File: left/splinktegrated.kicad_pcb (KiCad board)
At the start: 4 copper layers, 72.6 x 88.4 mm, 83 parts, among them J1 USB_C_Receptacle_USB2.0, J10 NA_Ribbon, J13 Conn_01x01_Socket, J14 Cirque, J15 Conn_01x01_Socket, J16 Conn_01x01_Socket, J17 Conn_01x01_Socket, J18 USB_C_Receptacle_USB2.0, J19 Conn_01x01_Socket, J20 Conn_01x01_Socket, J5 Conn_01x02, J6 Cirque, J7 NA_trackball, J8 NA_Ribbon, J9 NA_RGB, Q4 AO3401A, Q5 AO3401A, SW2 NA_SW_SPST, U1 RP2040, U2 USBLC6-2P6, U3 XC6210B332MR-G, U4 USBLC6-2P6, U5 W25Q128JVS, U6 74LVC1T45, Y1 Crystal_GND24

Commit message: vik logo
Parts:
- moved G*** 9.73 mm to (149.7, 130.2)
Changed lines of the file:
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@@
 	(footprint "LOGO"
 		(layer "F.Cu")
-		(at 159.35 130.95)
+		(at 149.65 130.18)
 		(property "Reference" "G***"
 			(at 0 0 0)

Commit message: routing
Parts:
- moved C6 0.17 mm to (156.5, 92.7)
- moved R6 0.16 mm to (157.8, 92.7)
- moved R7 0.16 mm to (159.1, 92.7)
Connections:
- J6 pad 10: SCL -> SDA
- J6 pad 9: SDA -> SCL
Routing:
- net SCL: track 49.6 -> 48.4 mm
- net SDA: track 49.7 -> 50.3 mm
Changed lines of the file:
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@@
 	(footprint "Resistor_SMD:R_0402_1005Metric"
 		(layer "F.Cu")
-		(at 157.8 92.53 -90)
+		(at 157.8 92.69 -90)
 		(descr "Resistor SMD 0402 (1005 Metric), square (rectangular) end terminal, IPC_7351 nominal, (Body size source: IPC-SM-782 page 72, https://www.pcb-3d.com/wordpress/wp-content/uploads/ipc-sm-782a_amendment_1_and_2.pdf), generated with kicad-footprint-generator")
 		(tags "resistor")
@@
 	(footprint "Resistor_SMD:R_0402_1005Metric"
 		(layer "F.Cu")
-		(at 159.1 92.85 -90)
+		(at 159.1 92.69 -90)
 		(descr "Resistor SMD 0402 (1005 Metric), square (rectangular) end terminal, IPC_7351 nominal, (Body size source: IPC-SM-782 page 72, https://www.pcb-3d.com/wordpress/wp-content/uploads/ipc-sm-782a_amendment_1_and_2.pdf), generated with kicad-footprint-generator")
 		(tags "resistor")
@@
 	(footprint "Capacitor_SMD:C_0402_1005Metric"
 		(layer "F.Cu")
-		(at 156.5 92.5 90)
+		(at 156.5 92.67 90)
 		(descr "Capacitor SMD 0402 (1005 Metric), square (rectangular) end terminal, IPC_7351 nominal, (Body size source: IPC-SM-782 page 76, https://www.pcb-3d.com/wordpress/wp-content/uploads/ipc-sm-782a_amendment_1_and_2.pdf), generated with kicad-footprint-generator")
 		(tags "capacitor")
@@
 			(size 0.28 1.25)
 			(layers "F.Cu" "F.Mask" "F.Paste")
-			(net 53 "SDA")
+			(net 54 "SCL")
 			(pinfunction "Pin_9")
 			(pintype "passive")
@@
 			(size 0.28 1.25)
 			(layers "F.Cu" "F.Mask" "F.Paste")
-			(net 54 "SCL")
+			(net 53 "SDA")
 			(pinfunction "Pin_10")
 			(pintype "passive")
@@
 			)
 		)
+		(property ki_fp_filters "MountingHole*Pad*")
+		(sheetname "/")
+		(sheetfile "splinktegrated.kicad_sch")
 		(attr exclude_from_pos_files dnp)
 		(fp_circle
@@
 			)
 		)
+		(property ki_fp_filters "Connector*:*_1x??_*")
+		(sheetname "/")
+		(sheetfile "splinktegrated.kicad_sch")
 		(attr through_hole exclude_from_pos_files exclude_from_bom dnp)
 		(fp_line
@@
 			)
 		)
+		(property ki_fp_filters "Connector*:*_1x??_*")
+		(sheetname "/")
+		(sheetfile "splinktegrated.kicad_sch")
 		(attr through_hole exclude_from_pos_files exclude_from_bom dnp)
 		(fp_line
@@
 			)
 		)
+		(property ki_fp_filters "MountingHole*Pad*")
+		(sheetname "/")
+		(sheetfile "splinktegrated.kicad_sch")
 		(attr exclude_from_pos_files dnp)
 		(fp_circle
@@
 			)
 		)
+		(property ki_fp_filters "Connector*:*_1x??_*")
+		(sheetname "/")
+		(sheetfile "splinktegrated.kicad_sch")
 		(attr through_hole exclude_from_pos_files exclude_from_bom dnp)
 		(fp_line
@@
 			)
 		)
+		(property ki_fp_filters "Connector*:*_1x??_*")
+		(sheetname "/")
+		(sheetfile "splinktegrated.kicad_sch")
 		(attr through_hole exclude_from_pos_files exclude_from_bom dnp)
 		(fp_line
@@
 	)
 	(segment
-		(start 156.185 131.915)
-		(end 156.185 130.8)
+		(start 156.685 131.415)
+		(end 156.685 130.8)
 		(width 0.11)
 		(layer "F.Cu")
@@
 	)
 	(segment
-		(start 150.8 96.6)
-		(end 150.4 97)
+		(start 156.5 131.6)
+		(end 156.685 131.415)
+		(width 0.11)
+		(layer "F.Cu")
+		(net 53)
+	)
+	(segment
+		(start 156.5 132.2)
+		(end 156.5 131.6)
 		(width 0.11)
 		(layer "F.Cu")
@@
 	)
 	(segment
-		(start 155.8 132.3)
-		(end 156.185 131.915)
+		(start 150.8 96.6)
+		(end 150.4 97)
 		(width 0.11)
 		(layer "F.Cu")
@@
 	)
 	(via
-		(at 155.8 132.3)
+		(at 156.5 132.2)
 		(size 0.45)
 		(drill 0.2)
@@
 	)
 	(segment
-		(start 145.8 127.3)
-		(end 147.7 129.2)
-		(width 0.11)
-		(layer "B.Cu")
-		(net 53)
-	)
-	(segment
-		(start 147.7 129.2)
-		(end 150.8 132.3)
+		(start 150.4 99.6)
+		(end 150.4 97)
 		(width 0.11)
 		(layer "B.Cu")
@@
 	)
 	(segment
-		(start 146.900001 103.6)
-		(end 148.4 103.6)
+		(start 149.3 100.7)
+		(end 150.4 99.6)
 		(width 0.11)
 		(layer "B.Cu")
@@
 	)
 	(segment
-		(start 145.8 104.7)
-		(end 145.8 119.5)
+		(start 145.8 127.3)
+		(end 145.8 104.7)
 		(width 0.11)
 		(layer "B.Cu")
@@
 	)
 	(segment
-		(start 150.4 99.6)
-		(end 150.4 97)
+		(start 150.8 132.3)
+		(end 145.8 127.3)
 		(width 0.11)
 		(layer "B.Cu")
@@
 	)
 	(segment
-		(start 145.8 119.5)
-		(end 145.8 127.1)
+		(start 156.4 132.3)
+		(end 150.8 132.3)
 		(width 0.11)
 		(layer "B.Cu")
@@
 	)
 	(segment
-		(start 149.3 100.7)
-		(end 150.4 99.6)
+		(start 145.8 104.7)
+		(end 146.900001 103.6)
 		(width 0.11)
 		(layer "B.Cu")
@@
 	)
 	(segment
-		(start 150.8 132.3)
-		(end 155.8 132.3)
+		(start 146.900001 103.6)
+		(end 148.4 103.6)
 		(width 0.11)
 		(layer "B.Cu")
@@
 	)
 	(segment
-		(start 146.4 104.1)
-		(end 146.900001 103.6)
+		(start 156.5 132.2)
+		(end 156.4 132.3)
 		(width 0.11)
 		(layer "B.Cu")
@@
 	)
 	(segment
-		(start 145.8 127.1)
-		(end 145.8 127.3)
+		(start 155.864293 131.855707)
+		(end 156.185 131.535)
 		(width 0.11)
-		(layer "B.Cu")
-		(net 53)
+		(layer "F.Cu")
+		(net 54)
 	)
 	(segment
-		(start 146.4 104.1)
-		(end 145.8 104.7)
-		(width 0.11)
-		(layer "B.Cu")
-		(net 53)
-	)
-	(segment
-		(start 156.685 132.215)
-		(end 156.685 130.8)
+		(start 155.459109 131.855707)
+		(end 155.864293 131.855707)
 		(width 0.11)
 		(layer "F.Cu")
@@
 	)
 	(segment
-		(start 156.6 132.3)
-		(end 156.685 132.215)
+		(start 156.185 131.535)
+		(end 156.185 130.8)
 		(width 0.11)
 		(layer "F.Cu")
@@
 	)
 	(via
-		(at 156.6 132.3)
+		(at 155.459109 131.855707)
 		(size 0.45)
 		(drill 0.2)
@@
 	)
 	(segment
-		(start 156.209 131.909)
-		(end 156.6 132.3)
-		(width 0.11)
-		(layer "B.Cu")
-		(net 54)
-	)
-	(segment
-		(start 146.991542 103.821)
-		(end 148.491541 103.821)
-		(width 0.11)
-		(layer "B.Cu")
-		(net 54)
-	)
-	(segment
-		(start 154.47 131.909)
-		(end 156.209 131.909)
-		(width 0.11)
-		(layer "B.Cu")
-		(net 54)
-	)
-	(segment
-		(start 150.7 99.612542)
-		(end 150.7 97.4)
-		(width 0.11)
-		(layer "B.Cu")
-		(net 54)
-	)
-	(segment
-		(start 148.491541 103.821)
-		(end 149.521 102.791542)
-		(width 0.11)
-		(layer "B.Cu")
-		(net 54)
-	)
-	(segment
-		(start 146.656271 104.156271)
-		(end 146.021 104.791542)
+		(start 150.891542 132.079)
+		(end 146.021 127.208458)
 		(width 0.11)
 		(layer "B.Cu")
@@
 	)
 	(segment
-		(start 146.021 127.2)
-		(end 146.021 127.208458)
+		(start 149.521 102.791542)
+		(end 149.521 100.791542)
 		(width 0.11)
 		(layer "B.Cu")
@@
 	)
 	(segment
-		(start 146.656271 104.156271)
+		(start 146.021 104.791542)
 		(end 146.991542 103.821)
 		(width 0.11)
@@
 	)
 	(segment
-		(start 154.3 132.079)
-		(end 154.47 131.909)
+		(start 155.235816 132.079)
+		(end 150.891542 132.079)
 		(width 0.11)
 		(layer "B.Cu")
@@
 	)
 	(segment
-		(start 149.521 102.791542)
-		(end 149.521 100.791542)
+		(start 155.459109 131.855707)
+		(end 155.235816 132.079)
 		(width 0.11)
 		(layer "B.Cu")
@@
 	)
 	(segment
-		(start 146.021 106.8)
-		(end 146.021 113.9)
+		(start 148.491541 103.821)
+		(end 149.521 102.791542)
 		(width 0.11)
 		(layer "B.Cu")
@@
 	)
 	(segment
-		(start 146.021 127.208458)
-		(end 146.406271 127.593729)
-		(width 0.11)
-		(layer "B.Cu")
-		(net 54)
-	)
-	(segment
-		(start 146.021 113.9)
-		(end 146.021 118.2)
-		(width 0.11)
-		(layer "B.Cu")
-		(net 54)
-	)
-	(segment
 		(start 150.7 97.4)
 		(end 151.1 97)
@@
 	)
 	(segment
-		(start 150.891542 132.079)
-		(end 154.3 132.079)
-		(width 0.11)
-		(layer "B.Cu")
-		(net 54)
-	)
-	(segment
-		(start 146.406271 127.593729)
-		(end 150.891542 132.079)
+		(start 146.991542 103.821)
+		(end 148.491541 103.821)
 		(width 0.11)
 		(layer "B.Cu")
@@
 	)
 	(segment
-		(start 146.021 104.791542)
-		(end 146.021 106.8)
+		(start 150.7 99.612542)
+		(end 150.7 97.4)
 		(width 0.11)
 		(layer "B.Cu")
@@
 	)
 	(segment
-		(start 146.021 118.2)
-		(end 146.021 127.2)
+		(start 146.021 127.208458)
+		(end 146.021 104.791542)
 		(width 0.11)
 		(layer "B.Cu")

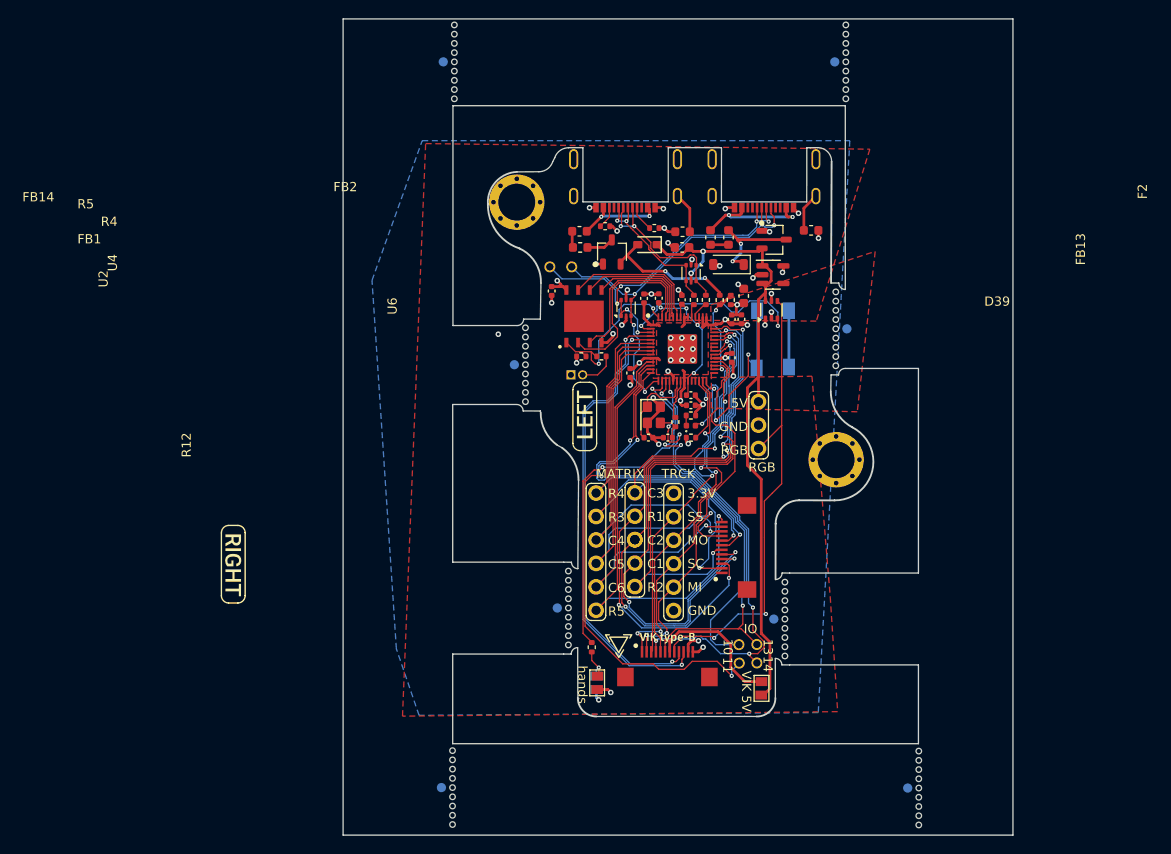
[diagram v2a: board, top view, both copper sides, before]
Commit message: remove outside panelling
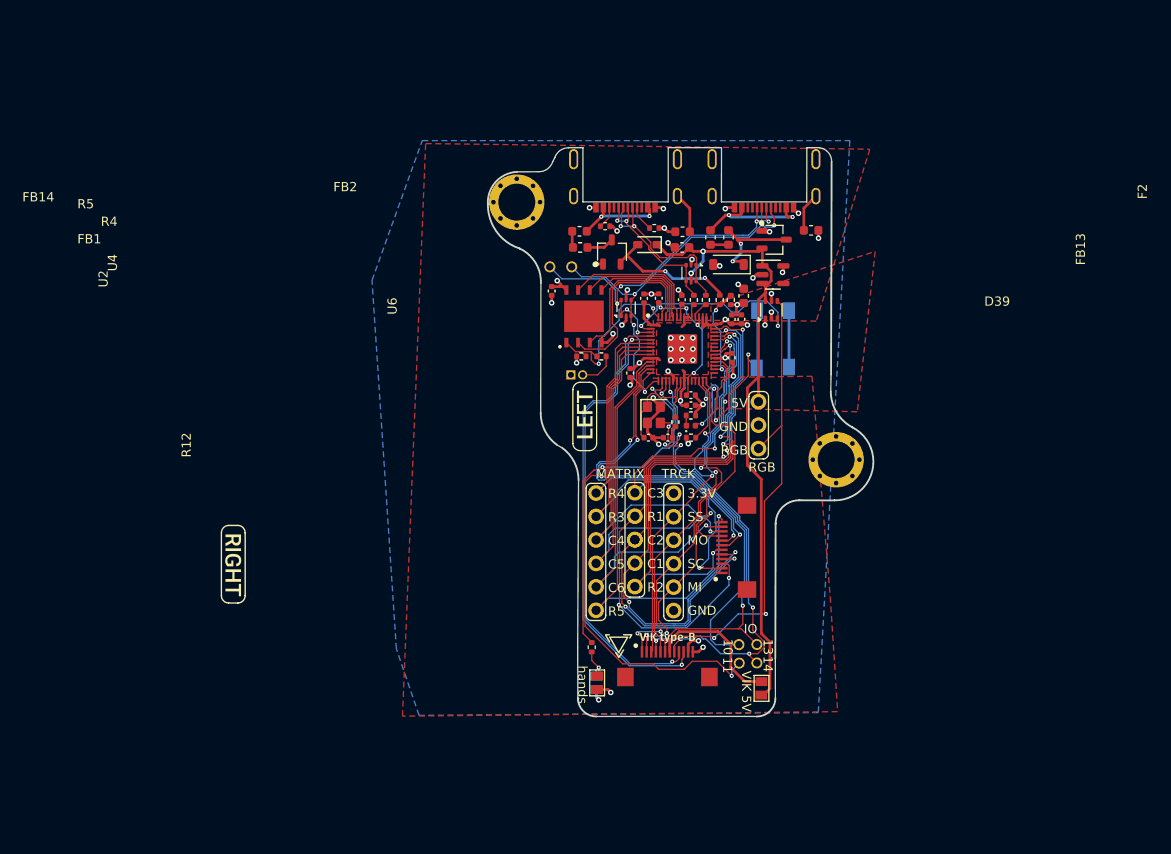
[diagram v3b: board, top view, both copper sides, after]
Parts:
- removed H5008 (x8): NA_M4, local-libraries:mousebite
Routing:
- net GND: vias 38 -> 37
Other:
- board size 72.6 x 88.4 mm -> 41.8 x 61.6 mm

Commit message: Revert "remove outside panelling"
This reverts commit 38a877c3f8acecfc4239cec6ccd43cc93e6b331c.
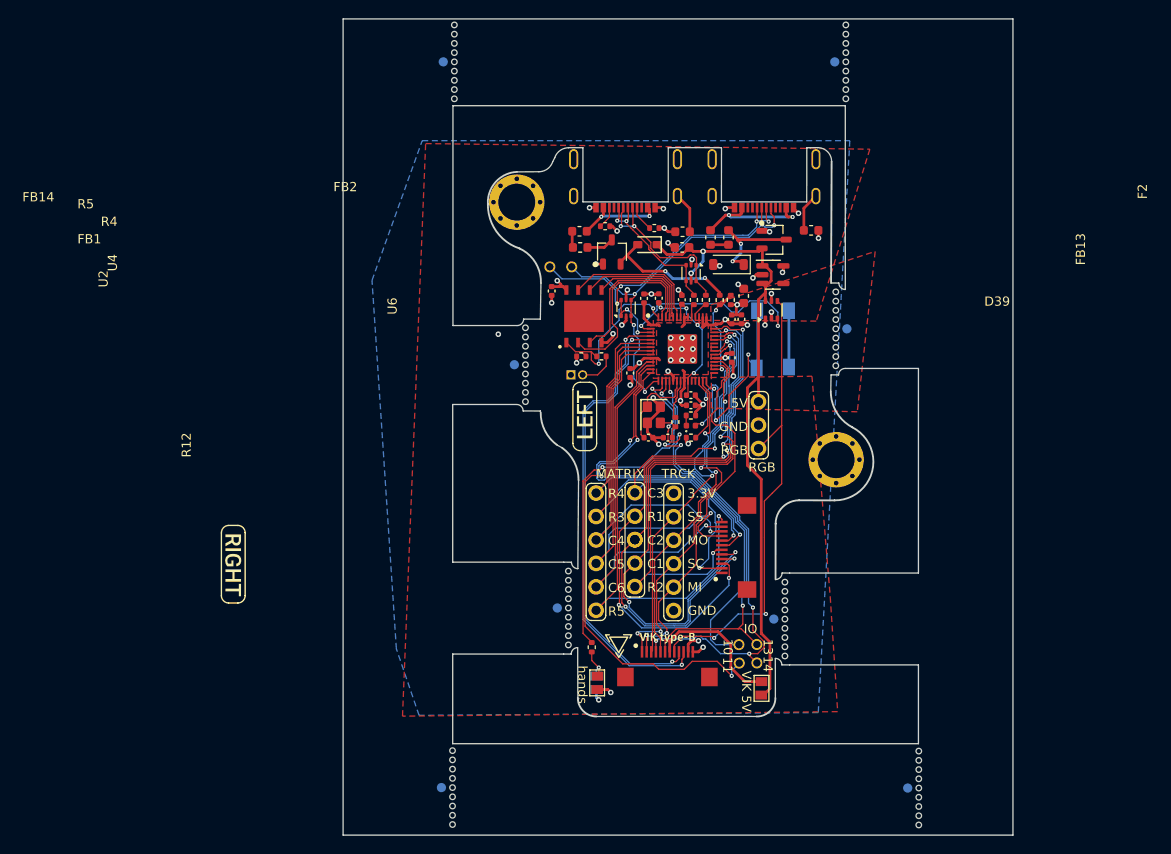
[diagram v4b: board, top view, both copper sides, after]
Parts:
- added H5008: NA_M4, local-libraries:mousebite, B.Cu at (139.6, 99.7)
- added H5008: NA_M4, local-libraries:mousebite, B.Cu at (131.9, 66.9)
- added H5008: NA_M4, local-libraries:mousebite, B.Cu at (174.3, 66.9)
- added H5008: NA_M4, local-libraries:mousebite, B.Cu at (144.2, 126.0)
- added H5008: NA_M4, local-libraries:mousebite, B.Cu at (173.2, 95.8)
- added H5008: NA_M4, local-libraries:mousebite, B.Cu at (182.2, 145.6)
- added H5008: NA_M4, local-libraries:mousebite, B.Cu at (167.7, 127.2)
- added H5008: NA_M4, local-libraries:mousebite, B.Cu at (131.7, 145.5)
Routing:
- net GND: vias 37 -> 38
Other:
- board size 41.8 x 61.6 mm -> 72.6 x 88.4 mm
